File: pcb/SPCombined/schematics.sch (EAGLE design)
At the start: 102 parts

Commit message: PCB size 2mm margin.
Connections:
- removed net GNDA: OIC3.EMIT, OID2.EMIT, OOA0.EMIT, OOA1.EMIT, OOD3.EMIT, OOD4.EMIT, OOD5.EMIT, T_12TO5_I.2, T_12TO5_O.2, T_CONV.1, T_LCD2.1, T_LCD_5V.2, T_LEAK1.2, T_LEAK2.2, T_MOT_SW1.2, T_MOT_SW2.2, T_RPM2.1, T_SW_G2.1, T_SW_G2.2, T_SW_R2.1, T_SW_R2.2, T_SW_Y2.1, T_SW_Y2.2
- net GND: now also OIC3.EMIT, OID2.EMIT, OOA0.EMIT, OOA1.EMIT, OOD3.EMIT, OOD4.EMIT, OOD5.EMIT, T_12TO5_I.2, T_12TO5_O.2, T_CONV.1, T_LCD2.1, T_LCD_5V.2, T_LEAK1.2, T_LEAK2.2, T_MOT_SW1.2, T_MOT_SW2.2, T_RPM2.1, T_SW_G2.1, T_SW_G2.2, T_SW_R2.1, T_SW_R2.2, T_SW_Y2.1, T_SW_Y2.2
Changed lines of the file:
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@@
 <wire x1="-124.46" y1="76.2" x2="-111.76" y2="76.2" width="0.1524" layer="91"/>
+</segment>
+<segment>
+<pinref part="OOD4" gate="A" pin="EMIT"/>
+<wire x1="137.16" y1="45.72" x2="132.08" y2="45.72" width="0.1524" layer="91"/>
+<pinref part="GNDI4" gate="1" pin="GND"/>
+</segment>
+<segment>
+<pinref part="OOD3" gate="A" pin="EMIT"/>
+<wire x1="134.62" y1="20.32" x2="129.54" y2="20.32" width="0.1524" layer="91"/>
+<pinref part="GNDI8" gate="1" pin="GND"/>
+</segment>
+<segment>
+<pinref part="OID2" gate="A" pin="EMIT"/>
+<wire x1="134.62" y1="-5.08" x2="129.54" y2="-5.08" width="0.1524" layer="91"/>
+<pinref part="GNDI11" gate="1" pin="GND"/>
+</segment>
+<segment>
+<pinref part="OIC3" gate="A" pin="EMIT"/>
+<wire x1="86.36" y1="-22.86" x2="86.36" y2="-17.78" width="0.1524" layer="91"/>
+<pinref part="GNDI12" gate="1" pin="GND"/>
+</segment>
+<segment>
+<pinref part="T_LEAK2" gate="G$1" pin="2"/>
+<wire x1="-119.38" y1="91.44" x2="-124.46" y2="91.44" width="0.1524" layer="91"/>
+<pinref part="GNDI15" gate="1" pin="GND"/>
+</segment>
+<segment>
+<pinref part="T_LEAK1" gate="G$1" pin="2"/>
+<wire x1="-119.38" y1="104.14" x2="-124.46" y2="104.14" width="0.1524" layer="91"/>
+<pinref part="GNDI16" gate="1" pin="GND"/>
+</segment>
+<segment>
+<pinref part="T_RPM2" gate="J$1" pin="1"/>
+<wire x1="-101.6" y1="-25.4" x2="-91.44" y2="-25.4" width="0.1524" layer="91"/>
+<pinref part="GNDI20" gate="1" pin="GND"/>
+</segment>
+<segment>
+<pinref part="T_LCD_5V" gate="G$1" pin="2"/>
+<wire x1="-119.38" y1="33.02" x2="-124.46" y2="33.02" width="0.1524" layer="91"/>
+<pinref part="GNDI19" gate="1" pin="GND"/>
+<wire x1="-119.38" y1="35.56" x2="-119.38" y2="33.02" width="0.1524" layer="91"/>
+</segment>
+<segment>
+<pinref part="T_12TO5_O" gate="G$1" pin="2"/>
+<wire x1="-119.38" y1="60.96" x2="-124.46" y2="60.96" width="0.1524" layer="91"/>
+<pinref part="GNDI17" gate="1" pin="GND"/>
+<wire x1="-119.38" y1="63.5" x2="-119.38" y2="60.96" width="0.1524" layer="91"/>
+</segment>
+<segment>
+<pinref part="T_12TO5_I" gate="G$1" pin="2"/>
+<wire x1="-119.38" y1="48.26" x2="-124.46" y2="48.26" width="0.1524" layer="91"/>
+<pinref part="GNDI18" gate="1" pin="GND"/>
+<wire x1="-119.38" y1="50.8" x2="-119.38" y2="48.26" width="0.1524" layer="91"/>
+</segment>
+<segment>
+<pinref part="T_CONV" gate="J$1" pin="1"/>
+<wire x1="-101.6" y1="-40.64" x2="-91.44" y2="-40.64" width="0.1524" layer="91"/>
+<pinref part="GNDI21" gate="1" pin="GND"/>
+</segment>
+<segment>
+<pinref part="T_MOT_SW1" gate="G$1" pin="2"/>
+<wire x1="-101.6" y1="104.14" x2="-93.98" y2="104.14" width="0.1524" layer="91"/>
+<pinref part="GNDI23" gate="1" pin="GND"/>
+</segment>
+<segment>
+<pinref part="T_MOT_SW2" gate="G$1" pin="2"/>
+<wire x1="-101.6" y1="91.44" x2="-93.98" y2="91.44" width="0.1524" layer="91"/>
+<pinref part="GNDI22" gate="1" pin="GND"/>
+<wire x1="-93.98" y1="93.98" x2="-93.98" y2="91.44" width="0.1524" layer="91"/>
+</segment>
+<segment>
+<wire x1="-73.66" y1="30.48" x2="-63.5" y2="30.48" width="0.1524" layer="91"/>
+<pinref part="GNDI25" gate="1" pin="GND"/>
+<pinref part="T_LCD2" gate="G$1" pin="1"/>
+</segment>
+<segment>
+<wire x1="-76.2" y1="58.42" x2="-66.04" y2="58.42" width="0.1524" layer="91"/>
+<wire x1="-76.2" y1="55.88" x2="-66.04" y2="55.88" width="0.1524" layer="91"/>
+<wire x1="-66.04" y1="58.42" x2="-66.04" y2="55.88" width="0.1524" layer="91"/>
+<pinref part="GNDI24" gate="1" pin="GND"/>
+<junction x="-66.04" y="55.88"/>
+<pinref part="T_SW_R2" gate="G$1" pin="1"/>
+<pinref part="T_SW_R2" gate="G$1" pin="2"/>
+</segment>
+<segment>
+<pinref part="OOA0" gate="A" pin="EMIT"/>
+<wire x1="-15.24" y1="76.2" x2="-15.24" y2="73.66" width="0.1524" layer="91"/>
+<pinref part="GNDI26" gate="1" pin="GND"/>
+</segment>
+<segment>
+<pinref part="OOA1" gate="A" pin="EMIT"/>
+<wire x1="10.16" y1="76.2" x2="10.16" y2="73.66" width="0.1524" layer="91"/>
+<pinref part="GNDI27" gate="1" pin="GND"/>
+</segment>
+<segment>
+<pinref part="OOD5" gate="A" pin="EMIT"/>
+<wire x1="137.16" y1="71.12" x2="132.08" y2="71.12" width="0.1524" layer="91"/>
+<pinref part="GNDI7" gate="1" pin="GND"/>
+</segment>
+<segment>
+<wire x1="-76.2" y1="78.74" x2="-66.04" y2="78.74" width="0.1524" layer="91"/>
+<wire x1="-76.2" y1="76.2" x2="-66.04" y2="76.2" width="0.1524" layer="91"/>
+<wire x1="-66.04" y1="78.74" x2="-66.04" y2="76.2" width="0.1524" layer="91"/>
+<pinref part="GNDI2" gate="1" pin="GND"/>
+<junction x="-66.04" y="76.2"/>
+<pinref part="T_SW_Y2" gate="G$1" pin="1"/>
+<pinref part="T_SW_Y2" gate="G$1" pin="2"/>
+</segment>
+<segment>
+<wire x1="-76.2" y1="99.06" x2="-66.04" y2="99.06" width="0.1524" layer="91"/>
+<wire x1="-76.2" y1="96.52" x2="-66.04" y2="96.52" width="0.1524" layer="91"/>
+<wire x1="-66.04" y1="99.06" x2="-66.04" y2="96.52" width="0.1524" layer="91"/>
+<pinref part="GNDI3" gate="1" pin="GND"/>
+<junction x="-66.04" y="96.52"/>
+<pinref part="T_SW_G2" gate="G$1" pin="1"/>
+<pinref part="T_SW_G2" gate="G$1" pin="2"/>
 </segment>
 </net>
@@
 </segment>
 </net>
-<net name="GNDA" class="0">
-<segment>
-<pinref part="OOD4" gate="A" pin="EMIT"/>
-<wire x1="137.16" y1="45.72" x2="132.08" y2="45.72" width="0.1524" layer="91"/>
-<pinref part="GNDI4" gate="1" pin="GND"/>
-</segment>
-<segment>
-<pinref part="OOD3" gate="A" pin="EMIT"/>
-<wire x1="134.62" y1="20.32" x2="129.54" y2="20.32" width="0.1524" layer="91"/>
-<pinref part="GNDI8" gate="1" pin="GND"/>
-</segment>
-<segment>
-<pinref part="OID2" gate="A" pin="EMIT"/>
-<wire x1="134.62" y1="-5.08" x2="129.54" y2="-5.08" width="0.1524" layer="91"/>
-<pinref part="GNDI11" gate="1" pin="GND"/>
-</segment>
-<segment>
-<pinref part="OIC3" gate="A" pin="EMIT"/>
-<wire x1="86.36" y1="-22.86" x2="86.36" y2="-17.78" width="0.1524" layer="91"/>
-<pinref part="GNDI12" gate="1" pin="GND"/>
-</segment>
-<segment>
-<pinref part="T_LEAK2" gate="G$1" pin="2"/>
-<wire x1="-119.38" y1="91.44" x2="-124.46" y2="91.44" width="0.1524" layer="91"/>
-<pinref part="GNDI15" gate="1" pin="GND"/>
-</segment>
-<segment>
-<pinref part="T_LEAK1" gate="G$1" pin="2"/>
-<wire x1="-119.38" y1="104.14" x2="-124.46" y2="104.14" width="0.1524" layer="91"/>
-<pinref part="GNDI16" gate="1" pin="GND"/>
-</segment>
-<segment>
-<pinref part="T_RPM2" gate="J$1" pin="1"/>
-<wire x1="-101.6" y1="-25.4" x2="-91.44" y2="-25.4" width="0.1524" layer="91"/>
-<pinref part="GNDI20" gate="1" pin="GND"/>
-</segment>
-<segment>
-<pinref part="T_LCD_5V" gate="G$1" pin="2"/>
-<wire x1="-119.38" y1="33.02" x2="-124.46" y2="33.02" width="0.1524" layer="91"/>
-<pinref part="GNDI19" gate="1" pin="GND"/>
-<wire x1="-119.38" y1="35.56" x2="-119.38" y2="33.02" width="0.1524" layer="91"/>
-</segment>
-<segment>
-<pinref part="T_12TO5_O" gate="G$1" pin="2"/>
-<wire x1="-119.38" y1="60.96" x2="-124.46" y2="60.96" width="0.1524" layer="91"/>
-<pinref part="GNDI17" gate="1" pin="GND"/>
-<wire x1="-119.38" y1="63.5" x2="-119.38" y2="60.96" width="0.1524" layer="91"/>
-</segment>
-<segment>
-<pinref part="T_12TO5_I" gate="G$1" pin="2"/>
-<wire x1="-119.38" y1="48.26" x2="-124.46" y2="48.26" width="0.1524" layer="91"/>
-<pinref part="GNDI18" gate="1" pin="GND"/>
-<wire x1="-119.38" y1="50.8" x2="-119.38" y2="48.26" width="0.1524" layer="91"/>
-</segment>
-<segment>
-<pinref part="T_CONV" gate="J$1" pin="1"/>
-<wire x1="-101.6" y1="-40.64" x2="-91.44" y2="-40.64" width="0.1524" layer="91"/>
-<pinref part="GNDI21" gate="1" pin="GND"/>
-</segment>
-<segment>
-<pinref part="T_MOT_SW1" gate="G$1" pin="2"/>
-<wire x1="-101.6" y1="104.14" x2="-93.98" y2="104.14" width="0.1524" layer="91"/>
-<pinref part="GNDI23" gate="1" pin="GND"/>
-</segment>
-<segment>
-<pinref part="T_MOT_SW2" gate="G$1" pin="2"/>
-<wire x1="-101.6" y1="91.44" x2="-93.98" y2="91.44" width="0.1524" layer="91"/>
-<pinref part="GNDI22" gate="1" pin="GND"/>
-<wire x1="-93.98" y1="93.98" x2="-93.98" y2="91.44" width="0.1524" layer="91"/>
-</segment>
-<segment>
-<wire x1="-73.66" y1="30.48" x2="-63.5" y2="30.48" width="0.1524" layer="91"/>
-<pinref part="GNDI25" gate="1" pin="GND"/>
-<pinref part="T_LCD2" gate="G$1" pin="1"/>
-</segment>
-<segment>
-<wire x1="-76.2" y1="58.42" x2="-66.04" y2="58.42" width="0.1524" layer="91"/>
-<wire x1="-76.2" y1="55.88" x2="-66.04" y2="55.88" width="0.1524" layer="91"/>
-<wire x1="-66.04" y1="58.42" x2="-66.04" y2="55.88" width="0.1524" layer="91"/>
-<pinref part="GNDI24" gate="1" pin="GND"/>
-<junction x="-66.04" y="55.88"/>
-<pinref part="T_SW_R2" gate="G$1" pin="1"/>
-<pinref part="T_SW_R2" gate="G$1" pin="2"/>
-</segment>
-<segment>
-<pinref part="OOA0" gate="A" pin="EMIT"/>
-<wire x1="-15.24" y1="76.2" x2="-15.24" y2="73.66" width="0.1524" layer="91"/>
-<pinref part="GNDI26" gate="1" pin="GND"/>
-</segment>
-<segment>
-<pinref part="OOA1" gate="A" pin="EMIT"/>
-<wire x1="10.16" y1="76.2" x2="10.16" y2="73.66" width="0.1524" layer="91"/>
-<pinref part="GNDI27" gate="1" pin="GND"/>
-</segment>
-<segment>
-<pinref part="OOD5" gate="A" pin="EMIT"/>
-<wire x1="137.16" y1="71.12" x2="132.08" y2="71.12" width="0.1524" layer="91"/>
-<pinref part="GNDI7" gate="1" pin="GND"/>
-</segment>
-<segment>
-<wire x1="-76.2" y1="78.74" x2="-66.04" y2="78.74" width="0.1524" layer="91"/>
-<wire x1="-76.2" y1="76.2" x2="-66.04" y2="76.2" width="0.1524" layer="91"/>
-<wire x1="-66.04" y1="78.74" x2="-66.04" y2="76.2" width="0.1524" layer="91"/>
-<pinref part="GNDI2" gate="1" pin="GND"/>
-<junction x="-66.04" y="76.2"/>
-<pinref part="T_SW_Y2" gate="G$1" pin="1"/>
-<pinref part="T_SW_Y2" gate="G$1" pin="2"/>
-</segment>
-<segment>
-<wire x1="-76.2" y1="99.06" x2="-66.04" y2="99.06" width="0.1524" layer="91"/>
-<wire x1="-76.2" y1="96.52" x2="-66.04" y2="96.52" width="0.1524" layer="91"/>
-<wire x1="-66.04" y1="99.06" x2="-66.04" y2="96.52" width="0.1524" layer="91"/>
-<pinref part="GNDI3" gate="1" pin="GND"/>
-<junction x="-66.04" y="96.52"/>
-<pinref part="T_SW_G2" gate="G$1" pin="1"/>
-<pinref part="T_SW_G2" gate="G$1" pin="2"/>
-</segment>
-</net>

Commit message: Rereroute.
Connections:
- net N$6 renamed +12VIN
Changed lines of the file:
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@@
 </segment>
 </net>
-<net name="N$6" class="0">
+<net name="+12VIN" class="0">
 <segment>
-<wire x1="-119.38" y1="81.28" x2="-119.38" y2="78.74" width="0.1524" layer="91"/>
+<wire x1="-114.3" y1="81.28" x2="-114.3" y2="78.74" width="0.1524" layer="91"/>
 <pinref part="T_12VIN" gate="G$1" pin="2"/>
-<wire x1="-119.38" y1="78.74" x2="-124.46" y2="78.74" width="0.1524" layer="91"/>
+<wire x1="-114.3" y1="78.74" x2="-124.46" y2="78.74" width="0.1524" layer="91"/>
 <pinref part="FUSE" gate="1" pin="1"/>
-<wire x1="-119.38" y1="81.28" x2="-114.3" y2="81.28" width="0.1524" layer="91"/>
+<label x="-124.46" y="78.74" size="1.778" layer="95"/>
 </segment>
 </net>

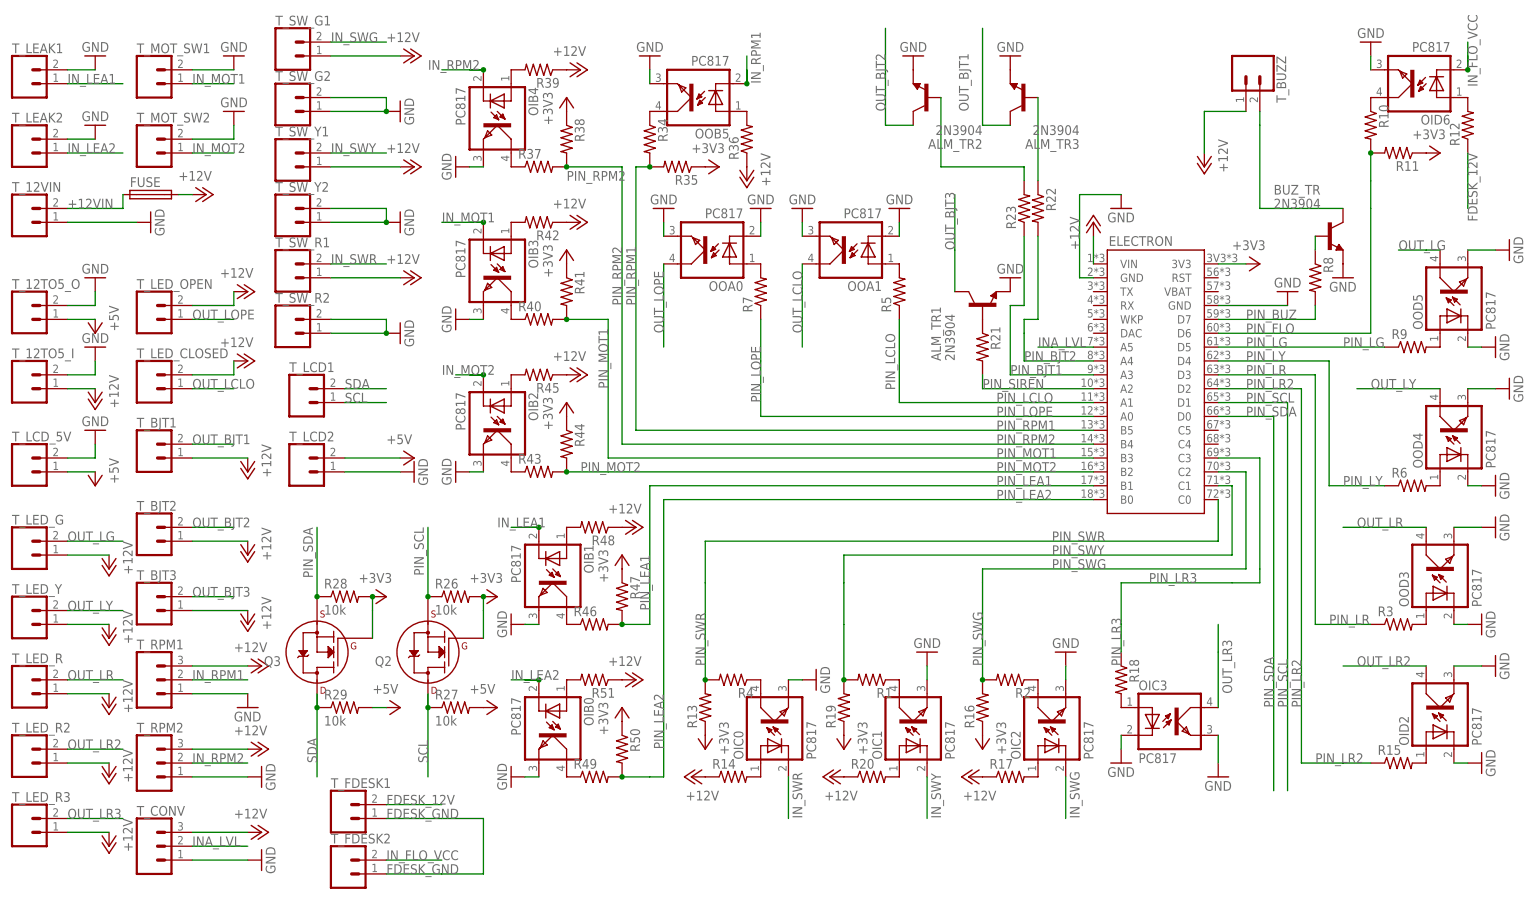
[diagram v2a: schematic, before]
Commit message: Add resistor values. Move out opto from electron area.
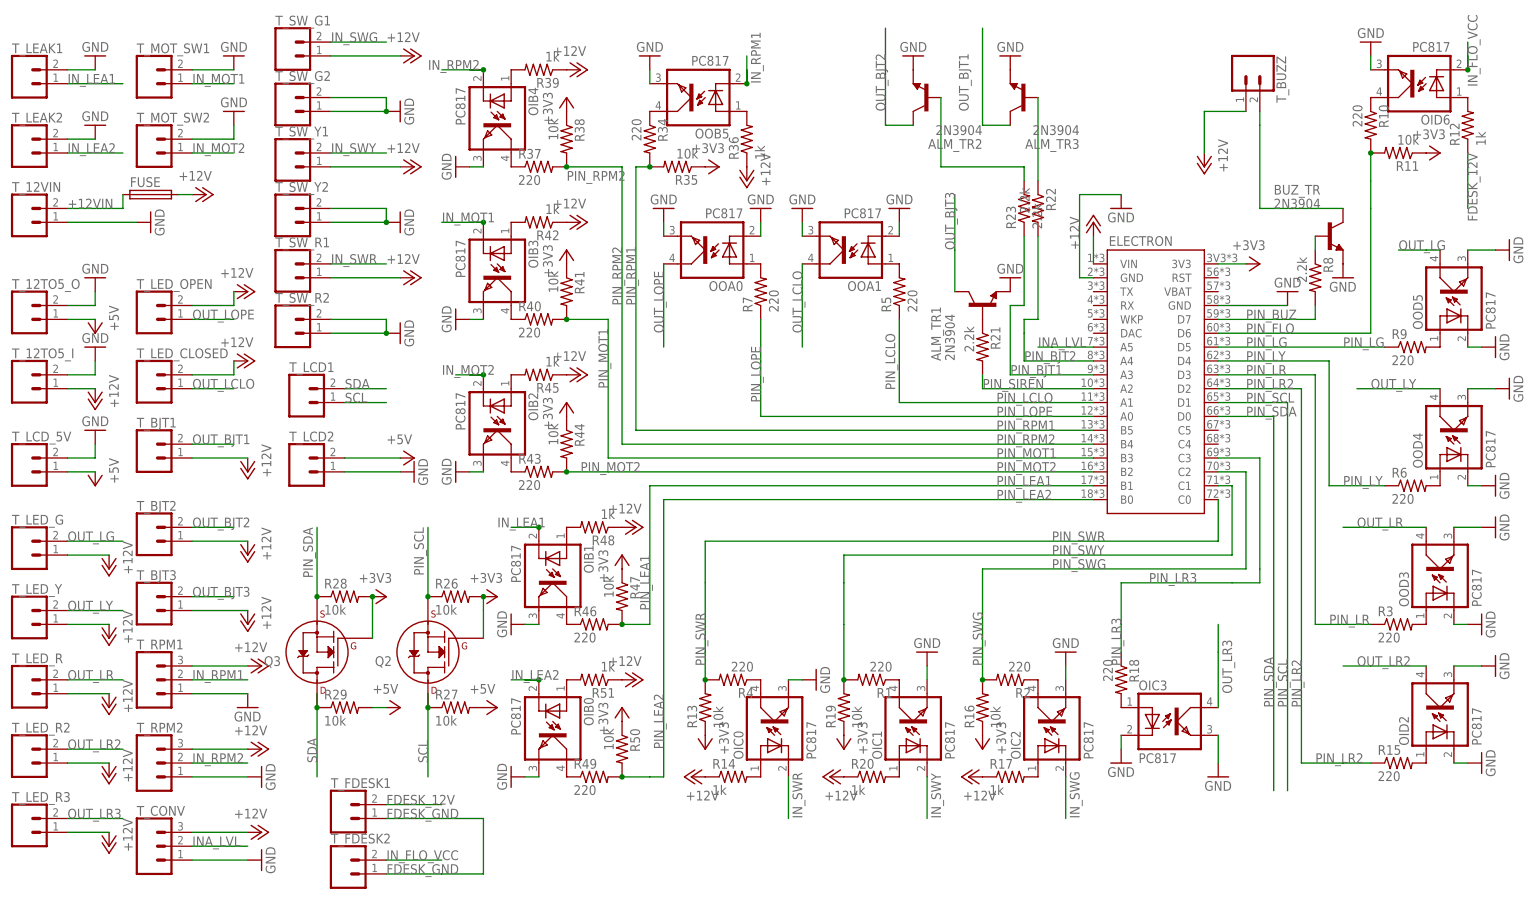
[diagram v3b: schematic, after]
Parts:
- R1, R10, R15, R18, R2, R3, R34, R37, R4, R40, R43, R46, R49, R5, R6, R7, R9: value (none) -> 220
- R11, R13, R16, R19, R35, R38, R41, R44, R47, R50: value (none) -> 10k
- R12, R14, R17, R20, R36, R39, R42, R45, R48, R51: value (none) -> 1k
- R21, R22, R23, R8: value (none) -> 2.2k
